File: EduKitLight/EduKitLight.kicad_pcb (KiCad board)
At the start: 2 copper layers, 8 parts, among them P1 CONN_01X05, P2 CONN_01X04, P3 CONN_01X02, P4 CONN_01X04, P5 CONN_01X05, P6 CONN_01X04, U1 uln2803A, U2 Arduino_Mini

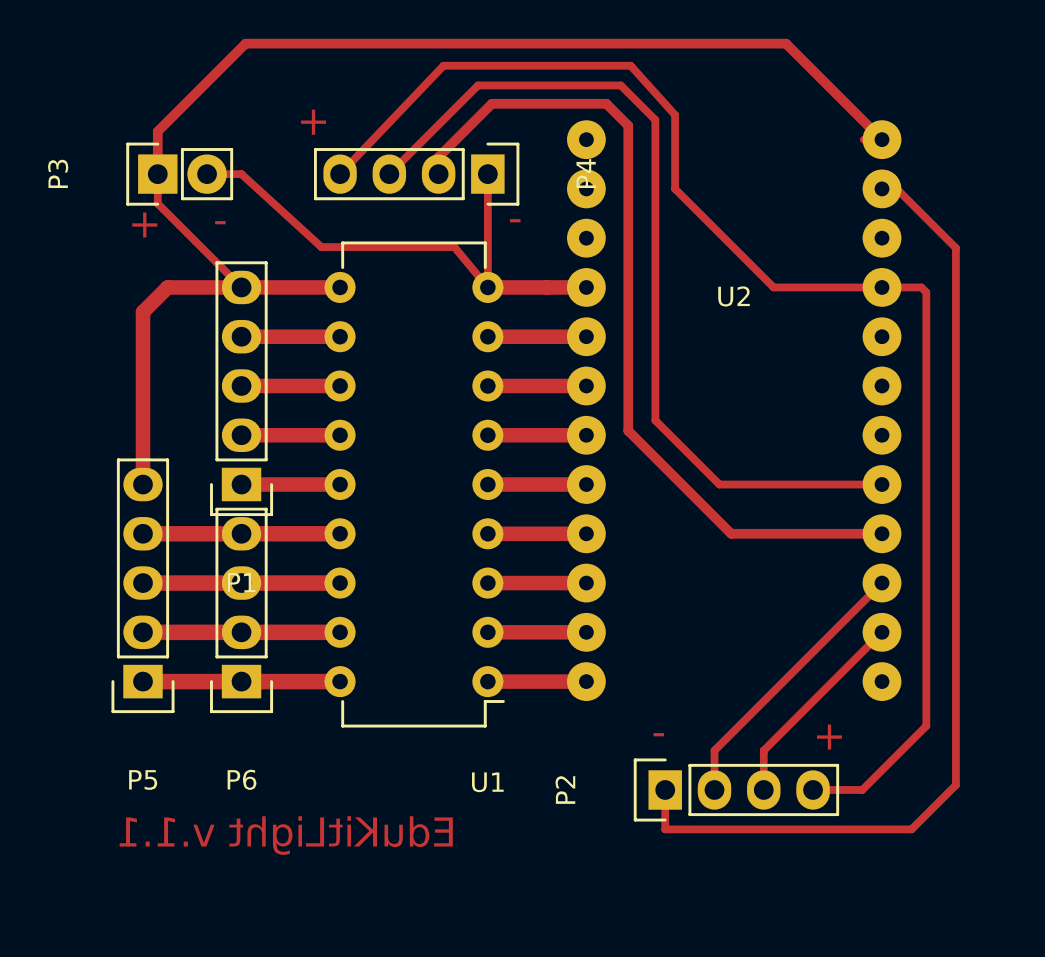
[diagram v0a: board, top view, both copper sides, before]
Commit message: Added subscriptions for PCB
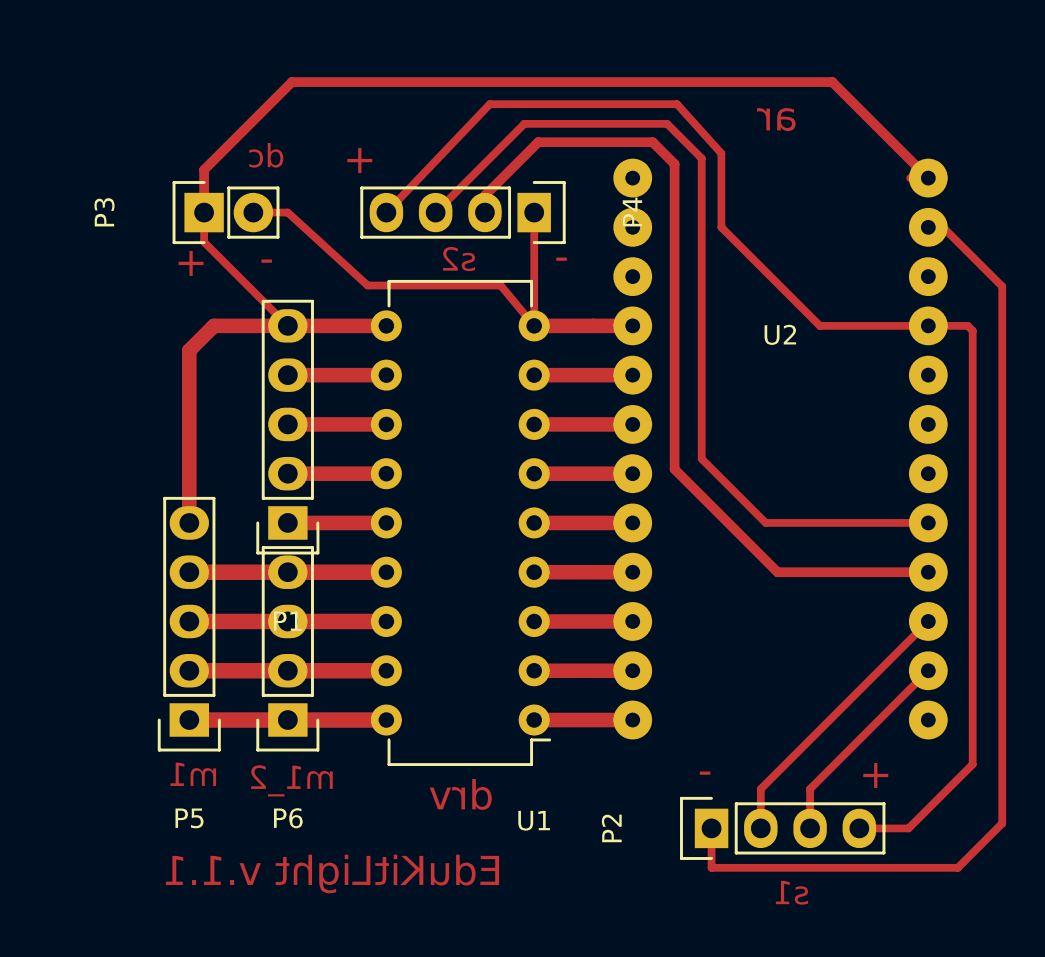
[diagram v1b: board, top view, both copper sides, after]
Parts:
- moved P3 3.10 mm to (19.7, 22.8)
- moved P1 3.10 mm to (24.0, 38.8)
- moved P4 3.10 mm to (36.7, 22.8)
- moved P5 3.10 mm to (18.9, 49.0)
- moved P6 3.10 mm to (24.0, 49.0)
- moved U1 3.10 mm to (36.7, 49.0)
- moved U2 3.10 mm to (49.4, 28.7)
- moved P2 3.10 mm to (45.8, 54.6)
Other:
- board text added: "ar"
- board text added: "dc"
- board text added: "drv"
- board text added: "m1"
- board text added: "m1_2"
- board text added: "s1"
- board text added: "s2"
